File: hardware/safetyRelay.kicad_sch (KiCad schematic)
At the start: 8 parts, among them K1 Relay_SPST-NO, Q3 S8050, SW2 SW_DPST_x2

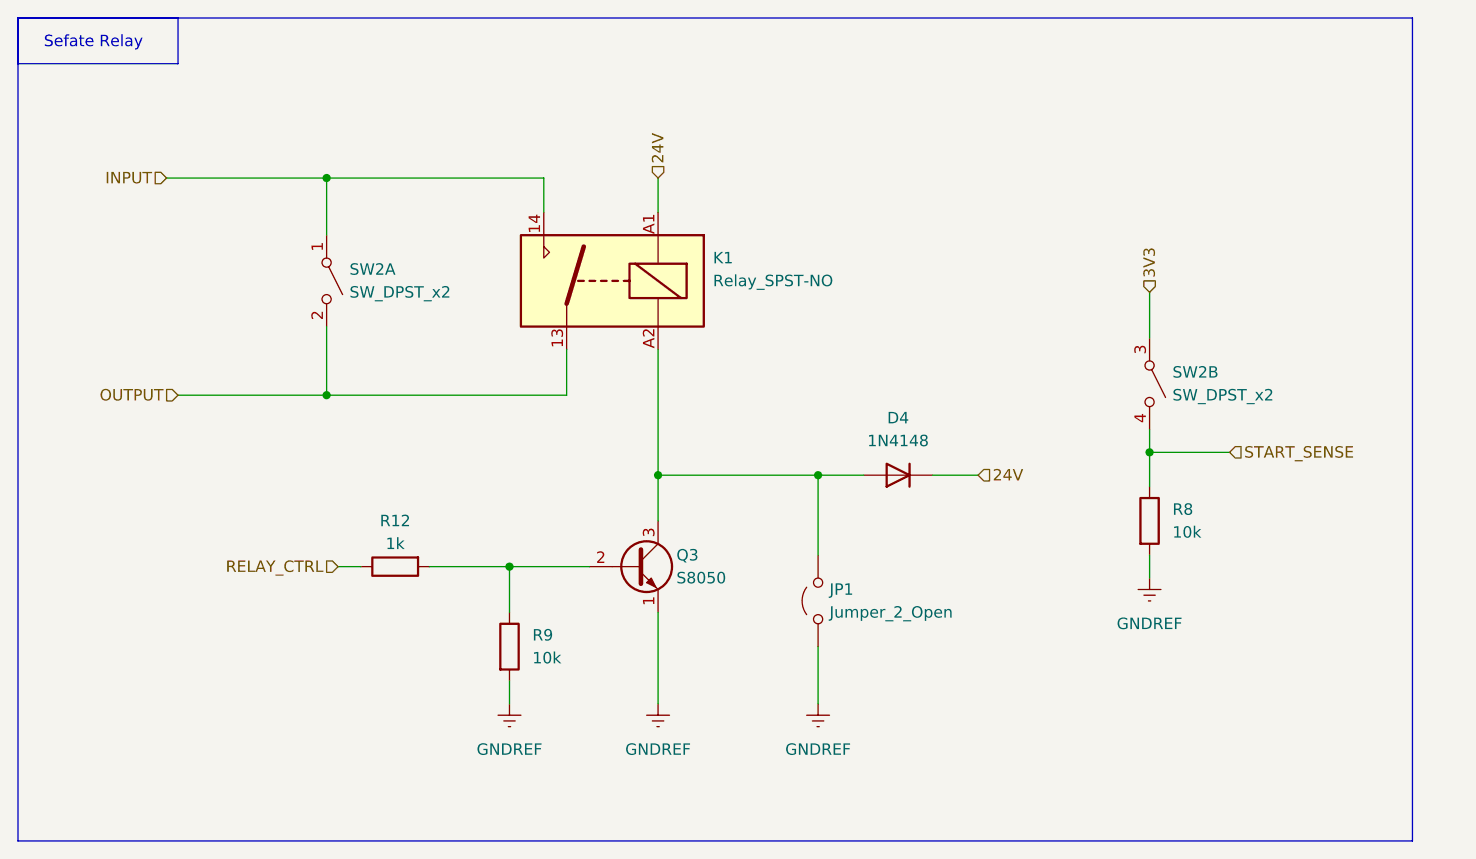
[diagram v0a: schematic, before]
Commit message: mvp
features:
	Logic Power Supply
	Safety Relay
	Main Unit
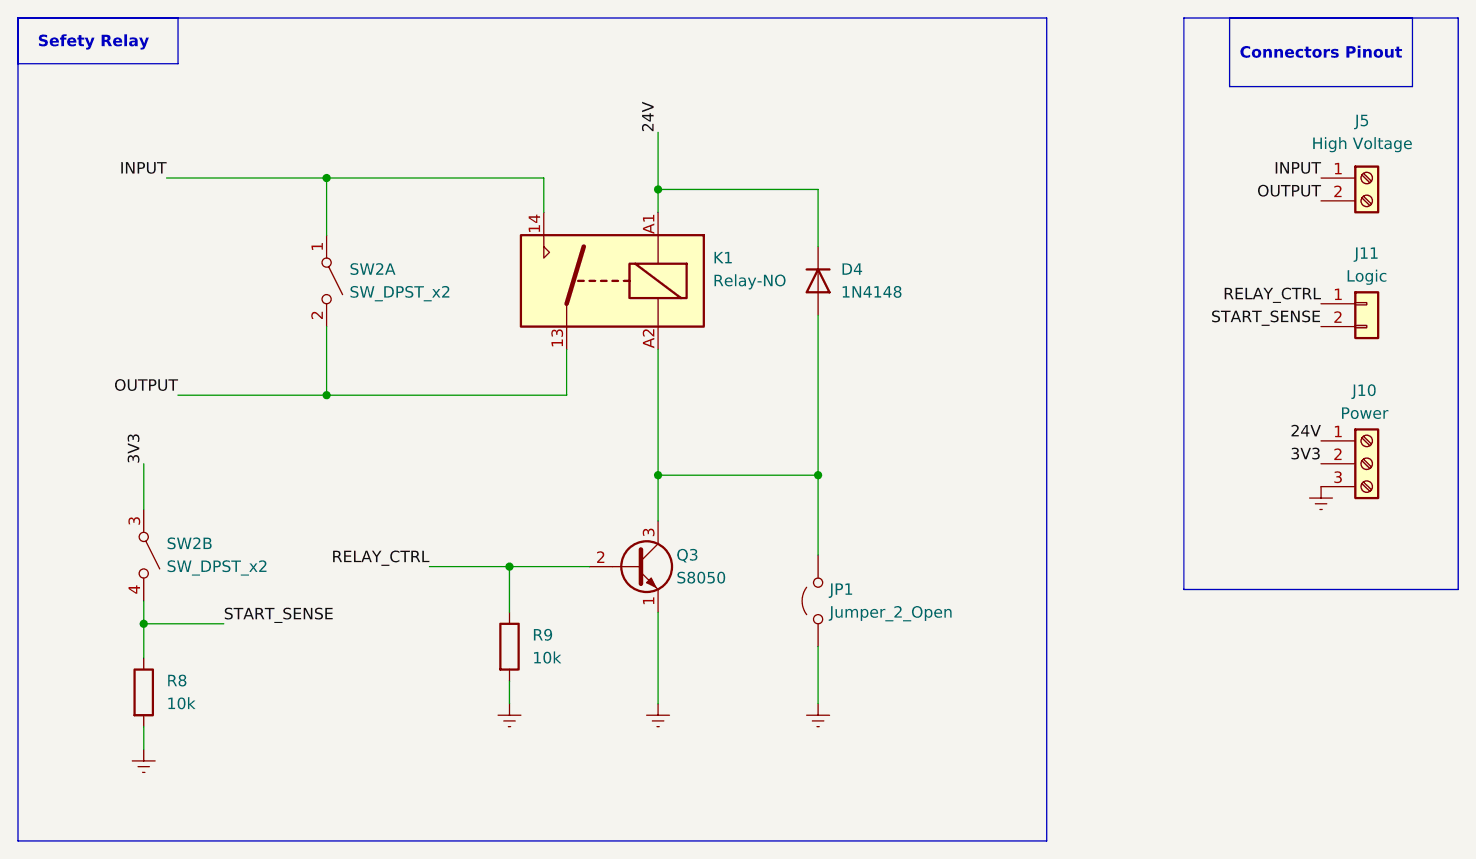
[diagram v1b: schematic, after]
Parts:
- removed R12: 1k, symbol Device:R
- added J10: Power, symbol Connector:Screw_Terminal_01x03
- added J11: Logic, symbol Connector_Generic:Conn_01x02
- added J5: High Voltage, symbol Connector:Screw_Terminal_01x02
- K1: value Relay_SPST-NO -> Relay-NO
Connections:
- net 24V: now also J10.1 (Pin_1)
- net 3V3: now also J10.2 (Pin_2)
- net GNDREF: now also J10.3 (Pin_3)
- net INPUT: now also J5.1 (Pin_1)
- net OUTPUT: now also J5.2 (Pin_2)
- net RELAY_CTRL: now also Q3.2 (B), R9.1, J11.1 (Pin_1)
- net START_SENSE: now also J11.2 (Pin_2)
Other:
- note added: "Connectors Pinout"
- note added: "Sefety Relay"
- note removed: "Sefate Relay"
- moved on the sheet: D4, R8, SW2B

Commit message: starting pcb
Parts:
- removed SW2: SW_DPST_x2, symbol Switch:SW_DPST_x2
- added J13: Relay Contact, TerminalBlock:TerminalBlock_MaiXu_MX126-5.0-02P_1x02_P5.00mm, symbol Connector:Screw_Terminal_01x02
- added J14: Relay Coil, TerminalBlock:TerminalBlock_MaiXu_MX126-5.0-02P_1x02_P5.00mm, symbol Connector:Screw_Terminal_01x02
- added SW2: SW_SPST, TerminalBlock:TerminalBlock_MaiXu_MX126-5.0-02P_1x02_P5.00mm, symbol Switch:SW_SPST
- added SW3: SW_SPST, Connector_PinHeader_2.54mm:PinHeader_1x02_P2.54mm_Vertical, symbol Switch:SW_SPST
- D4: footprint Diode_THT:D_DO-35_SOD27_P7.62mm_Horizontal -> Diode_SMD:D_SOD-123F
- J10: footprint (none) -> TerminalBlock:TerminalBlock_MaiXu_MX126-5.0-03P_1x03_P5.00mm
- J11: footprint (none) -> Connector_PinHeader_2.54mm:PinHeader_1x02_P2.54mm_Vertical
- J5: footprint (none) -> TerminalBlock:TerminalBlock_MaiXu_MX126-5.0-02P_1x02_P5.00mm
- JP1: footprint (none) -> Connector_PinHeader_2.54mm:PinHeader_1x03_P2.54mm_Vertical
- K1: footprint (none) -> TerminalBlock:TerminalBlock_MaiXu_MX126-5.0-04P_1x04_P5.00mm
- Q3: footprint Package_TO_SOT_THT:TO-92_Inline -> Package_TO_SOT_SMD:SOT-23-3
- R8, R9: footprint (none) -> Resistor_SMD:R_0603_1608Metric
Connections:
- net 24V: now also J14.2 (Pin_2)
- net 3V3: now also SW3.1 (A)
- net INPUT: now also J5.2 (Pin_2), J13.1 (Pin_1), SW2.1 (A); no longer J5.1 (Pin_1)
- net OUTPUT: now also J5.1 (Pin_1), J13.2 (Pin_2), SW2.2 (B); no longer J5.2 (Pin_2)
- net START_SENSE: now also SW3.2 (B)
- net at D4.2 (A), JP1.2 (B), K1.A2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: now also J14.1 (Pin_1)
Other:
- moved on the sheet: D4, JP1, K1, Q3, R8, R9

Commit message: last
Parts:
- D4: LCSC (none) -> C2128
- Q3: value S8050 -> 2N2222; footprint Package_TO_SOT_SMD:SOT-23-3 -> Package_TO_SOT_THT:TO-92_Inline; LCSC (none) -> C2146
- R8, R9: footprint Resistor_SMD:R_0603_1608Metric -> Resistor_SMD:R_0805_2012Metric_Pad1.20x1.40mm_HandSolder; LCSC (none) -> C25804
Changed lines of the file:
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@@
+			)
+		)
+		(property "LCSC" ""
+			(at 175.26 52.07 0)
+			(hide yes)
+			(show_name no)
+			(do_not_autoplace no)
+			(effects
+				(font
+					(size 1.27 1.27)
+				)
 			)
 		)
@@
 			)
 		)
+		(property "LCSC" ""
+			(at 91.44 41.91 0)
+			(hide yes)
+			(show_name no)
+			(do_not_autoplace no)
+			(effects
+				(font
+					(size 1.27 1.27)
+				)
+			)
+		)
 		(pin "A2"
 		)
@@
 			)
 		)
-		(property "Footprint" "Resistor_SMD:R_0603_1608Metric"
+		(property "Footprint" "Resistor_SMD:R_0805_2012Metric_Pad1.20x1.40mm_HandSolder"
 			(at 78.232 67.31 90)
 			(hide yes)
@@
 			)
 		)
+		(property "LCSC" "C25804"
+			(at 80.01 67.31 0)
+			(hide yes)
+			(show_name no)
+			(do_not_autoplace no)
+			(effects
+				(font
+					(size 1.27 1.27)
+				)
+			)
+		)
 		(pin "2"
 		)
@@
 			)
 		)
+		(property "LCSC" ""
+			(at 175.26 69.85 0)
+			(hide yes)
+			(show_name no)
+			(do_not_autoplace no)
+			(effects
+				(font
+					(size 1.27 1.27)
+				)
+			)
+		)
 		(pin "1"
 		)
@@
 			)
 		)
-		(property "Value" "S8050"
+		(property "Value" "2N2222"
 			(at 98.552 62.23 0)
 			(show_name no)
@@
 			)
 		)
-		(property "Footprint" "Package_TO_SOT_SMD:SOT-23-3"
+		(property "Footprint" "Package_TO_SOT_THT:TO-92_Inline"
 			(at 99.06 62.865 0)
 			(hide yes)
@@
 		)
 		(property "Description" "0.7A Ic, 20V Vce, Low Voltage High Current NPN Transistor, TO-92"
+			(at 93.98 60.96 0)
+			(hide yes)
+			(show_name no)
+			(do_not_autoplace no)
+			(effects
+				(font
+					(size 1.27 1.27)
+				)
+			)
+		)
+		(property "LCSC" "C2146"
 			(at 93.98 60.96 0)
 			(hide yes)
@@
 			)
 		)
+		(property "LCSC" ""
+			(at 114.3 60.96 90)
+			(hide yes)
+			(show_name no)
+			(do_not_autoplace no)
+			(effects
+				(font
+					(size 1.27 1.27)
+				)
+			)
+		)
 		(pin "2"
 		)
@@
 		)
 		(property "Description" "Generic screw terminal, single row, 01x02, script generated (kicad-library-utils/schlib/autogen/connector/)"
+			(at 175.26 38.1 0)
+			(hide yes)
+			(show_name no)
+			(do_not_autoplace no)
+			(effects
+				(font
+					(size 1.27 1.27)
+				)
+			)
+		)
+		(property "LCSC" ""
 			(at 175.26 38.1 0)
 			(hide yes)
@@
 			)
 		)
+		(property "LCSC" "C2128"
+			(at 114.3 41.91 90)
+			(hide yes)
+			(show_name no)
+			(do_not_autoplace no)
+			(effects
+				(font
+					(size 1.27 1.27)
+				)
+			)
+		)
 		(pin "2"
 		)
@@
 			)
 		)
+		(property "LCSC" ""
+			(at 73.66 41.91 0)
+			(hide yes)
+			(show_name no)
+			(do_not_autoplace no)
+			(effects
+				(font
+					(size 1.27 1.27)
+				)
+			)
+		)
 		(pin "1"
 		)
@@
 			)
 		)
-		(property "Footprint" "Resistor_SMD:R_0603_1608Metric"
+		(property "Footprint" "Resistor_SMD:R_0805_2012Metric_Pad1.20x1.40mm_HandSolder"
 			(at 55.88 77.978 90)
 			(hide yes)
@@
 			)
 		)
+		(property "LCSC" "C25804"
+			(at 55.88 76.2 90)
+			(hide yes)
+			(show_name no)
+			(do_not_autoplace no)
+			(effects
+				(font
+					(size 1.27 1.27)
+				)
+			)
+		)
 		(pin "2"
 		)
@@
 			)
 		)
+		(property "LCSC" ""
+			(at 41.91 76.2 0)
+			(hide yes)
+			(show_name no)
+			(do_not_autoplace no)
+			(effects
+				(font
+					(size 1.27 1.27)
+				)
+			)
+		)
 		(pin "1"
 		)
@@
 		(property "Description" "Single Pole Single Throw (SPST) switch"
 			(at 49.53 41.91 0)
+			(hide yes)
+			(show_name no)
+			(do_not_autoplace no)
+			(effects
+				(font
+					(size 1.27 1.27)
+				)
+			)
+		)
+		(property "LCSC" ""
+			(at 49.53 41.91 90)
 			(hide yes)
 			(show_name no)
@@
 			(at 105.41 40.64 0)
 			(hide yes)
+			(show_name no)
+			(do_not_autoplace no)
+			(effects
+				(font
+					(size 1.27 1.27)
+				)
+			)
+		)
+		(property "LCSC" ""
+			(at 105.41 40.64 0)
+			(hide yes)
